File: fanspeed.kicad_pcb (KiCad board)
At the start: 2 copper layers, 35.6 x 27.9 mm, 16 parts, among them J1 Conn_01x02_Female, J2 Conn_01x04_Female, Q1 2N3904, Q2 2N3904, Q3 2N3904, U1 PC847

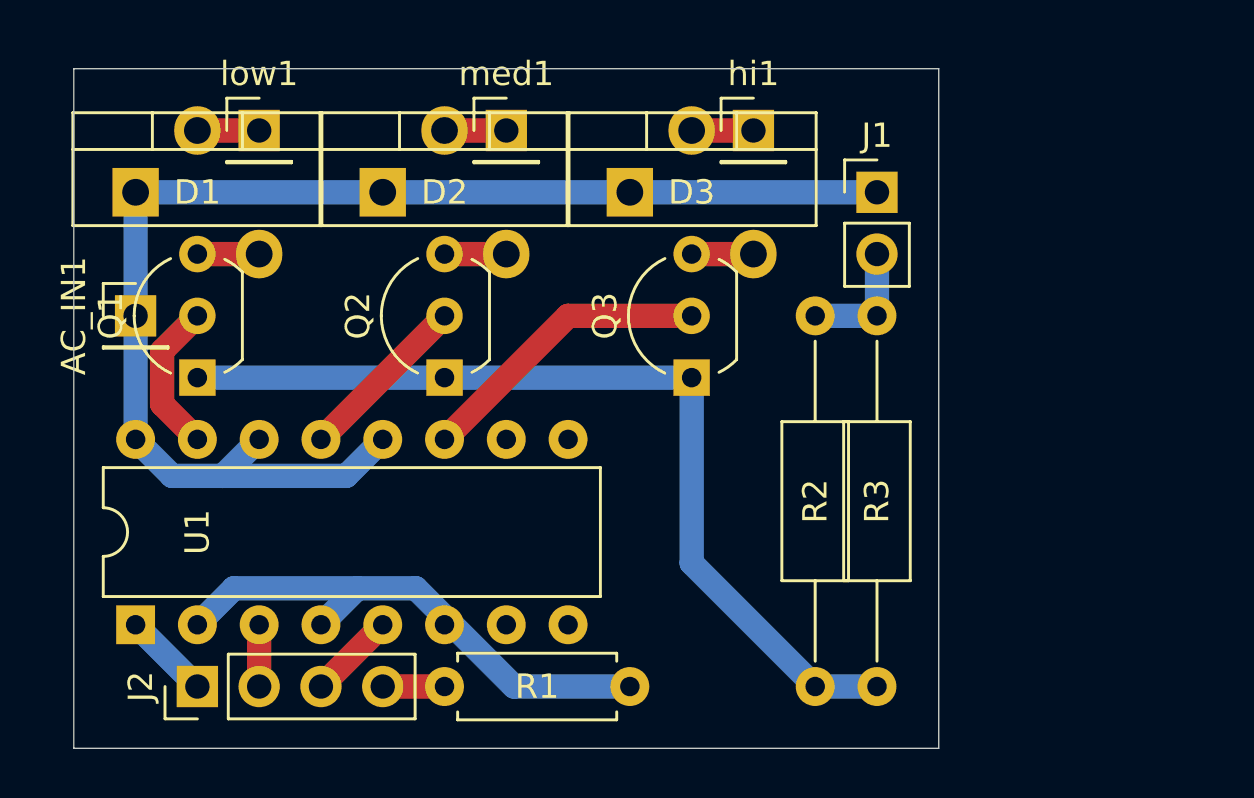
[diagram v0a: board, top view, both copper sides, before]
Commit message: Switched to opto-triacs
Upgraded KiCAD from 5 to 6
Using the load as the current-liming resistor to simplify wiring
Upgraded connectors to screw-terminals
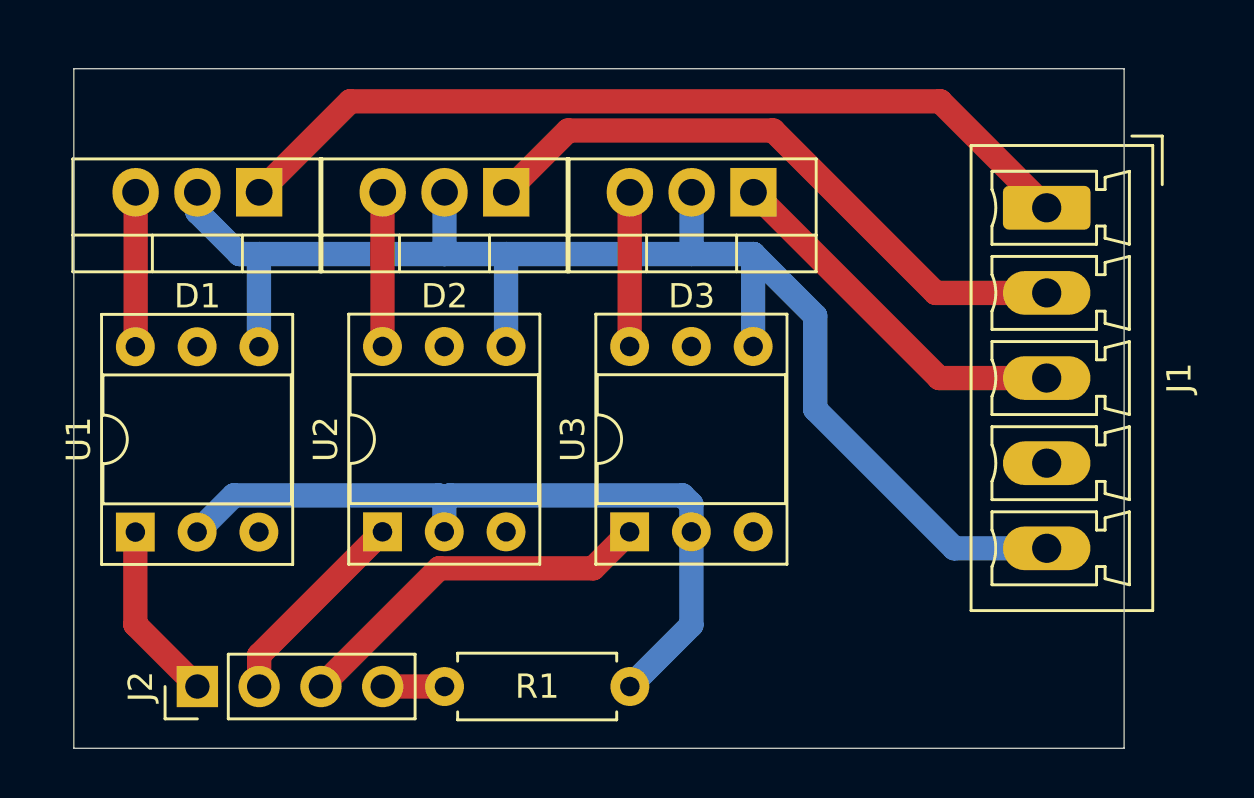
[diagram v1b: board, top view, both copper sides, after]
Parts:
- removed AC_IN1, hi1, low1, med1: Conn_01x01_Female, Connector_PinHeader_2.54mm:PinHeader_1x01_P2.54mm_Vertical
- removed Q1, Q2, Q3: 2N3904, Package_TO_SOT_THT:TO-92_Inline_Wide
- removed R2, R3: 120, Resistor_THT:R_Axial_DIN0207_L6.3mm_D2.5mm_P15.24mm_Horizontal
- added U2: MOC3023M, Package_DIP:DIP-6_W7.62mm_Socket, F.Cu at (124.5, 95.2)
- added U3: MOC3023M, Package_DIP:DIP-6_W7.62mm_Socket, F.Cu at (134.6, 95.2)
- D1, D2, D3: footprint fanspeed:TO-220-3_Offset -> Package_TO_SOT_THT:TO-220-3_Vertical
- J1: value Conn_01x02_Female -> Conn_01x05; footprint Connector_PinHeader_2.54mm:PinHeader_1x02_P2.54mm_Vertical -> Connector_Phoenix_MC:PhoenixContact_MCV_1,5_5-G-3.5_1x05_P3.50mm_Vertical
- U1: value PC847 -> MOC3023M; footprint Package_DIP:DIP-16_W7.62mm -> Package_DIP:DIP-6_W7.62mm_Socket
- moved J1 7.01 mm to (151.8, 81.9), turned to -90 degrees
- moved D1 5.08 mm to (119.4, 81.3), turned to 180 degrees
- moved D2 5.08 mm to (129.5, 81.3), turned to 180 degrees
- moved D3 5.08 mm to (139.7, 81.3), turned to 180 degrees
- moved U1 3.81 mm to (114.3, 95.2)
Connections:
- D1 pad 1: Net-(AC_IN1-Pad1) -> Net-(D1-Pad1)
- D1 pad 3: Net-(D1-Pad3) -> Net-(U1-Pad6)
- D2 pad 1: Net-(AC_IN1-Pad1) -> Net-(D2-Pad1)
- D2 pad 2: Net-(D2-Pad2) -> Net-(D1-Pad2)
- D3 pad 1: Net-(AC_IN1-Pad1) -> Net-(D3-Pad1)
- D3 pad 2: Net-(D3-Pad2) -> Net-(D1-Pad2)
- J1 pad 1: Net-(AC_IN1-Pad1) -> Net-(D1-Pad1)
- J1 pad 2: Net-(J1-Pad2) -> Net-(D2-Pad1)
- U1 pad 3: Net-(J2-Pad2) -> unconnected-(U1-Pad3)
- U1 pad 4: Net-(R1-Pad1) -> Net-(D1-Pad2)
- U1 pad 5: Net-(J2-Pad3) -> unconnected-(U1-Pad5)
- U1 pad 6: Net-(R1-Pad1) -> Net-(U1-Pad6)
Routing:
- net Net-(D1-Pad2): track 2.54 -> 60.2 mm
- net Net-(AC_IN1-Pad1): track 54.2 -> 0.00 mm
- net Net-(Q1-Pad1): track 37.7 -> 0.00 mm
- net Net-(D1-Pad1): track 0.00 -> 35.7 mm
- net Net-(D2-Pad1): track 0.00 -> 26.0 mm
- net Net-(D3-Pad1): track 0.00 -> 15.2 mm
- net Net-(Q3-Pad2): track 12.3 -> 0.00 mm
- net Net-(J2-Pad3): track 3.59 -> 15.3 mm
- net Net-(R1-Pad1): track 22.2 -> 31.1 mm
- net Net-(Q2-Pad2): track 7.18 -> 0.00 mm
- net Net-(U1-Pad6): track 0.00 -> 6.35 mm
- net Net-(Q1-Pad2): track 6.28 -> 0.00 mm
- net Net-(J2-Pad2): track 2.54 -> 8.46 mm
- net Net-(J1-Pad2): track 5.08 -> 0.00 mm
- net Net-(J2-Pad1): track 3.59 -> 7.41 mm
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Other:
- board size 35.6 x 27.9 mm -> 43.2 x 27.9 mm
- net class Default removed
